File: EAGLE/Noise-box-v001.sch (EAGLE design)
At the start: 20 parts, among them J1 AVR_SPI_PROG_3X22X3_LOCK, J2 BATT, U1 ATMEGA328P_TQFP, U2 MIC5219 3.3V, U3 MCP73831

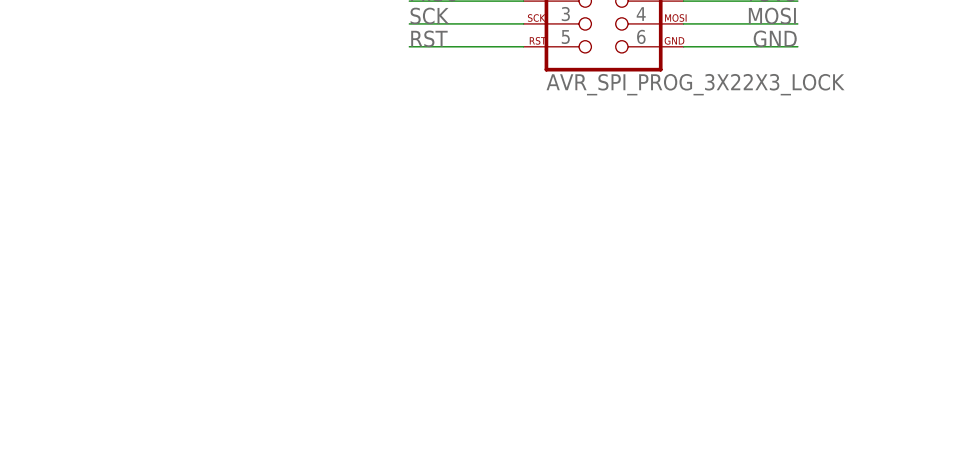
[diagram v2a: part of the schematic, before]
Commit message: Low voltage rail
Added 1.8V rail to accomodate codec IC core
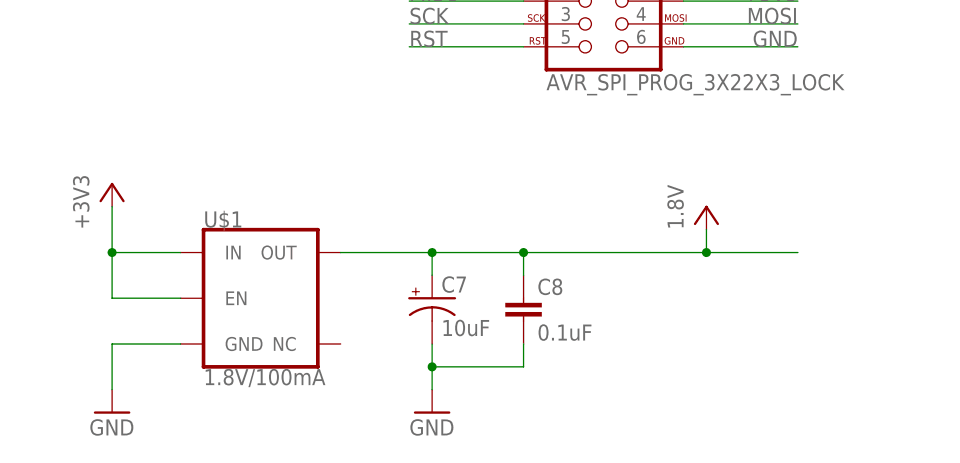
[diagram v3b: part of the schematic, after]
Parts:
- added C7: 10uF, SparkFun-Capacitors:10UF-POLAR-EIA3216-16V-10%(TANT)
- added C8: 0.1uF, SparkFun-Capacitors:0.1UF-0603-25V-5%
- added U$1: 1.8V/100mA, SparkFun-IC-Power:V_REG_SP6214-1.8V
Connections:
- new net VCC: C7.+, C8.1, U$1.OUT
- net +3V3: now also U$1.EN, U$1.IN
- net GND: now also C7.-, C8.2, U$1.GND
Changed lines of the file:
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@@
 <part name="GND7" library="supply1" deviceset="GND" device=""/>
 <part name="GND8" library="supply1" deviceset="GND" device=""/>
+<part name="U$1" library="SparkFun-IC-Power" deviceset="V_REG_SP6214" device="-1.8V" value="1.8V/100mA"/>
+<part name="C7" library="SparkFun-Capacitors" deviceset="10UF-POLAR" device="-EIA3216-16V-10%(TANT)" value="10uF"/>
+<part name="C8" library="SparkFun-Capacitors" deviceset="0.1UF" device="-0603-25V-5%" value="0.1uF"/>
+<part name="GND9" library="supply1" deviceset="GND" device=""/>
+<part name="GND10" library="supply1" deviceset="GND" device=""/>
+<part name="+3V3" library="supply1" deviceset="+3V3" device=""/>
+<part name="P+2" library="supply1" deviceset="VCC" device="" value="1.8V"/>
 </parts>
 <sheets>
@@
 <instance part="GND7" gate="1" x="55.88" y="198.12"/>
 <instance part="GND8" gate="1" x="83.82" y="198.12"/>
+<instance part="U$1" gate="G$1" x="30.48" y="139.7"/>
+<instance part="C7" gate="G$1" x="48.26" y="139.7"/>
+<instance part="C8" gate="G$1" x="58.42" y="137.16"/>
+<instance part="GND9" gate="1" x="12.7" y="127"/>
+<instance part="GND10" gate="1" x="48.26" y="127"/>
+<instance part="+3V3" gate="G$1" x="12.7" y="152.4"/>
+<instance part="P+2" gate="VCC" x="78.74" y="149.86"/>
 </instances>
 <busses>
@@
 <junction x="132.08" y="256.54"/>
 </segment>
+<segment>
+<pinref part="+3V3" gate="G$1" pin="+3V3"/>
+<pinref part="U$1" gate="G$1" pin="IN"/>
+<wire x1="12.7" y1="149.86" x2="12.7" y2="144.78" width="0.1524" layer="91"/>
+<wire x1="12.7" y1="144.78" x2="20.32" y2="144.78" width="0.1524" layer="91"/>
+<pinref part="U$1" gate="G$1" pin="EN"/>
+<wire x1="20.32" y1="139.7" x2="12.7" y2="139.7" width="0.1524" layer="91"/>
+<wire x1="12.7" y1="139.7" x2="12.7" y2="144.78" width="0.1524" layer="91"/>
+<junction x="12.7" y="144.78"/>
+</segment>
 </net>
 <net name="GND" class="0">
@@
 <wire x1="111.76" y1="200.66" x2="101.6" y2="200.66" width="0.1524" layer="91"/>
 <junction x="101.6" y="200.66"/>
+</segment>
+<segment>
+<pinref part="C7" gate="G$1" pin="-"/>
+<pinref part="GND10" gate="1" pin="GND"/>
+<wire x1="48.26" y1="134.62" x2="48.26" y2="132.08" width="0.1524" layer="91"/>
+<pinref part="C8" gate="G$1" pin="2"/>
+<wire x1="48.26" y1="132.08" x2="48.26" y2="129.54" width="0.1524" layer="91"/>
+<wire x1="58.42" y1="134.62" x2="58.42" y2="132.08" width="0.1524" layer="91"/>
+<wire x1="58.42" y1="132.08" x2="48.26" y2="132.08" width="0.1524" layer="91"/>
+<junction x="48.26" y="132.08"/>
+</segment>
+<segment>
+<pinref part="U$1" gate="G$1" pin="GND"/>
+<pinref part="GND9" gate="1" pin="GND"/>
+<wire x1="20.32" y1="134.62" x2="12.7" y2="134.62" width="0.1524" layer="91"/>
+<wire x1="12.7" y1="134.62" x2="12.7" y2="129.54" width="0.1524" layer="91"/>
 </segment>
 </net>
@@
 </segment>
 </net>
+<net name="VCC" class="0">
+<segment>
+<pinref part="U$1" gate="G$1" pin="OUT"/>
+<wire x1="38.1" y1="144.78" x2="48.26" y2="144.78" width="0.1524" layer="91"/>
+<pinref part="C7" gate="G$1" pin="+"/>
+<wire x1="48.26" y1="144.78" x2="58.42" y2="144.78" width="0.1524" layer="91"/>
+<wire x1="58.42" y1="144.78" x2="78.74" y2="144.78" width="0.1524" layer="91"/>
+<wire x1="78.74" y1="144.78" x2="88.9" y2="144.78" width="0.1524" layer="91"/>
+<wire x1="48.26" y1="142.24" x2="48.26" y2="144.78" width="0.1524" layer="91"/>
+<junction x="48.26" y="144.78"/>
+<pinref part="C8" gate="G$1" pin="1"/>
+<wire x1="58.42" y1="142.24" x2="58.42" y2="144.78" width="0.1524" layer="91"/>
+<junction x="58.42" y="144.78"/>
+<pinref part="P+2" gate="VCC" pin="VCC"/>
+<wire x1="78.74" y1="144.78" x2="78.74" y2="147.32" width="0.1524" layer="91"/>
+<junction x="78.74" y="144.78"/>
+</segment>
+</net>

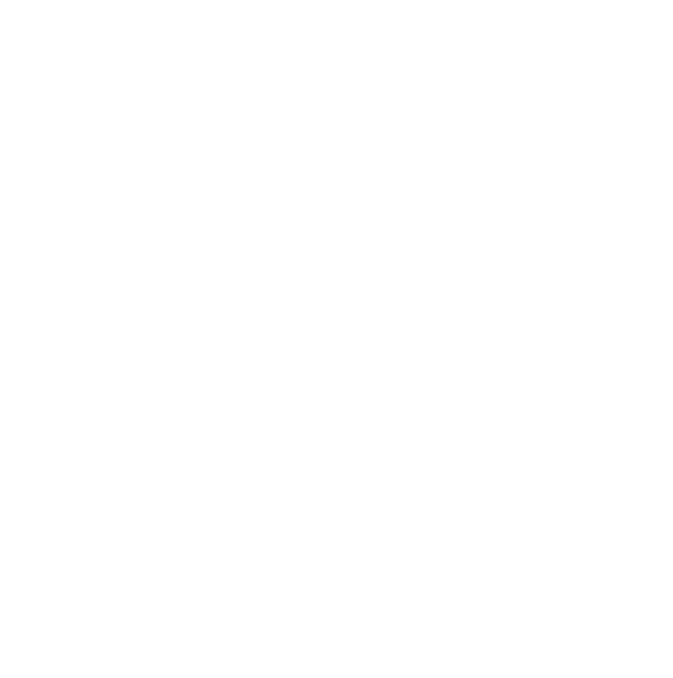
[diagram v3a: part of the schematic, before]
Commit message: micro sd
Added micro sd socket, to hold music tracks
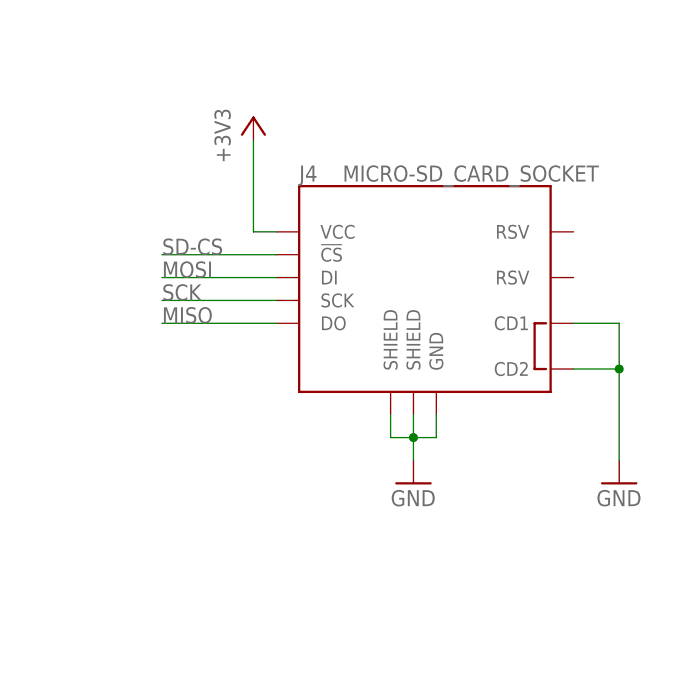
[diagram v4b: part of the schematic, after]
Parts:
- added J4: MICRO-SD_CARD_SOCKET, SparkFun-Connectors:MICRO-SD_CARD_SOCKET
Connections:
- new net SD-CS: J4.!CS
- net +3V3: now also J4.VCC
- net GND: now also J4.CD1, J4.CD2, J4.GND, J4.SHIELD@1, J4.SHIELD@3
- net MISO: now also J4.DO
- net MOSI: now also J4.DI
- net SCK: now also J4.SCK
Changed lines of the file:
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@@
 <part name="+3V3" library="supply1" deviceset="+3V3" device=""/>
 <part name="P+2" library="supply1" deviceset="VCC" device="" value="1.8V"/>
+<part name="J4" library="SparkFun-Connectors" deviceset="MICRO-SD_CARD_SOCKET" device=""/>
+<part name="+3V4" library="supply1" deviceset="+3V3" device=""/>
+<part name="GND11" library="supply1" deviceset="GND" device=""/>
+<part name="GND12" library="supply1" deviceset="GND" device=""/>
 </parts>
 <sheets>
@@
 <instance part="+3V3" gate="G$1" x="12.7" y="152.4"/>
 <instance part="P+2" gate="VCC" x="78.74" y="149.86"/>
+<instance part="J4" gate="1" x="294.64" y="243.84"/>
+<instance part="+3V4" gate="G$1" x="276.86" y="261.62"/>
+<instance part="GND11" gate="1" x="294.64" y="220.98"/>
+<instance part="GND12" gate="1" x="317.5" y="220.98"/>
 </instances>
 <busses>
@@
 <junction x="12.7" y="144.78"/>
 </segment>
+<segment>
+<pinref part="J4" gate="1" pin="VCC"/>
+<wire x1="279.4" y1="248.92" x2="276.86" y2="248.92" width="0.1524" layer="91"/>
+<wire x1="276.86" y1="248.92" x2="276.86" y2="259.08" width="0.1524" layer="91"/>
+<pinref part="+3V4" gate="G$1" pin="+3V3"/>
+</segment>
 </net>
 <net name="GND" class="0">
@@
 <wire x1="12.7" y1="134.62" x2="12.7" y2="129.54" width="0.1524" layer="91"/>
 </segment>
+<segment>
+<pinref part="J4" gate="1" pin="SHIELD@3"/>
+<pinref part="GND11" gate="1" pin="GND"/>
+<wire x1="294.64" y1="228.6" x2="294.64" y2="226.06" width="0.1524" layer="91"/>
+<pinref part="J4" gate="1" pin="GND"/>
+<wire x1="294.64" y1="226.06" x2="294.64" y2="223.52" width="0.1524" layer="91"/>
+<wire x1="297.18" y1="228.6" x2="297.18" y2="226.06" width="0.1524" layer="91"/>
+<wire x1="297.18" y1="226.06" x2="294.64" y2="226.06" width="0.1524" layer="91"/>
+<junction x="294.64" y="226.06"/>
+<pinref part="J4" gate="1" pin="SHIELD@1"/>
+<wire x1="292.1" y1="228.6" x2="292.1" y2="226.06" width="0.1524" layer="91"/>
+<wire x1="292.1" y1="226.06" x2="294.64" y2="226.06" width="0.1524" layer="91"/>
+</segment>
+<segment>
+<pinref part="J4" gate="1" pin="CD1"/>
+<pinref part="GND12" gate="1" pin="GND"/>
+<wire x1="312.42" y1="238.76" x2="317.5" y2="238.76" width="0.1524" layer="91"/>
+<wire x1="317.5" y1="238.76" x2="317.5" y2="233.68" width="0.1524" layer="91"/>
+<pinref part="J4" gate="1" pin="CD2"/>
+<wire x1="317.5" y1="233.68" x2="317.5" y2="223.52" width="0.1524" layer="91"/>
+<wire x1="312.42" y1="233.68" x2="317.5" y2="233.68" width="0.1524" layer="91"/>
+<junction x="317.5" y="233.68"/>
+</segment>
 </net>
 <net name="MOSI" class="0">
@@
 <label x="88.9" y="170.18" size="1.778" layer="95" rot="MR0"/>
 </segment>
+<segment>
+<pinref part="J4" gate="1" pin="DI"/>
+<wire x1="279.4" y1="243.84" x2="266.7" y2="243.84" width="0.1524" layer="91"/>
+<label x="266.7" y="243.84" size="1.778" layer="95"/>
+</segment>
 </net>
 <net name="RST" class="0">
@@
 <label x="45.72" y="170.18" size="1.778" layer="95"/>
 </segment>
+<segment>
+<pinref part="J4" gate="1" pin="SCK"/>
+<wire x1="279.4" y1="241.3" x2="266.7" y2="241.3" width="0.1524" layer="91"/>
+<label x="266.7" y="241.3" size="1.778" layer="95"/>
+</segment>
 </net>
 <net name="MISO" class="0">
@@
 <wire x1="58.42" y1="172.72" x2="45.72" y2="172.72" width="0.1524" layer="91"/>
 <label x="45.72" y="172.72" size="1.778" layer="95"/>
+</segment>
+<segment>
+<pinref part="J4" gate="1" pin="DO"/>
+<wire x1="279.4" y1="238.76" x2="266.7" y2="238.76" width="0.1524" layer="91"/>
+<label x="266.7" y="238.76" size="1.778" layer="95"/>
 </segment>
 </net>
@@
 </segment>
 </net>
+<net name="SD-CS" class="0">
+<segment>
+<pinref part="J4" gate="1" pin="!CS"/>
+<wire x1="279.4" y1="246.38" x2="266.7" y2="246.38" width="0.1524" layer="91"/>
+<label x="266.7" y="246.38" size="1.778" layer="95"/>
+</segment>
+</net>

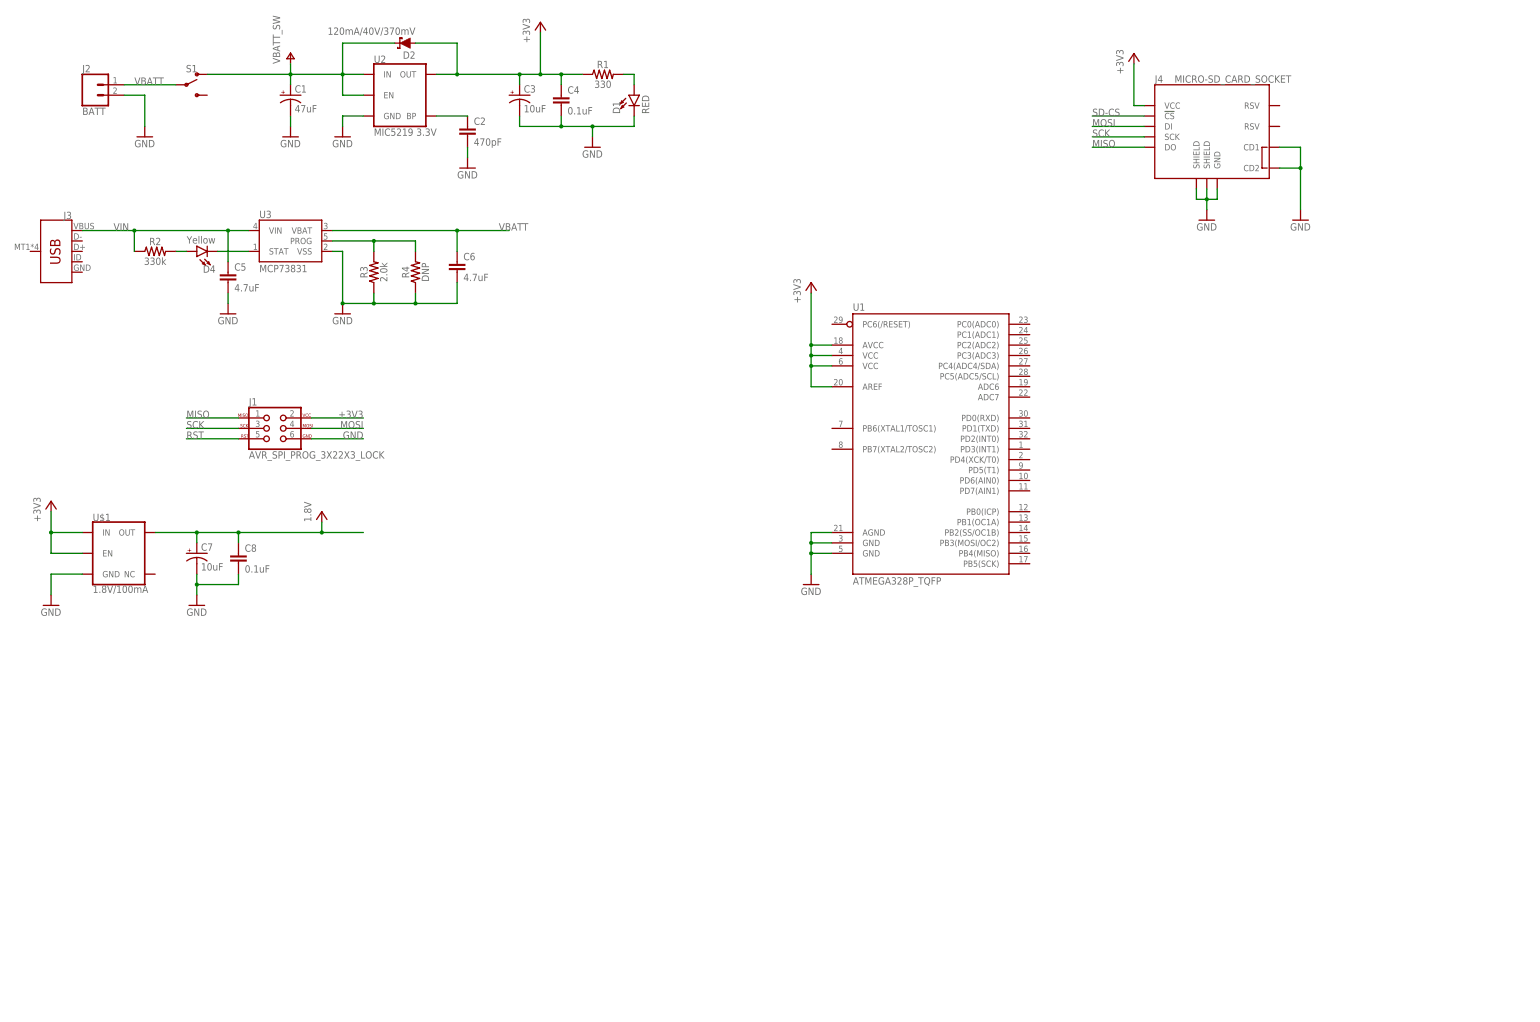
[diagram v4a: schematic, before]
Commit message: mp3 decoder
Added VL1063 codec, headphone jack
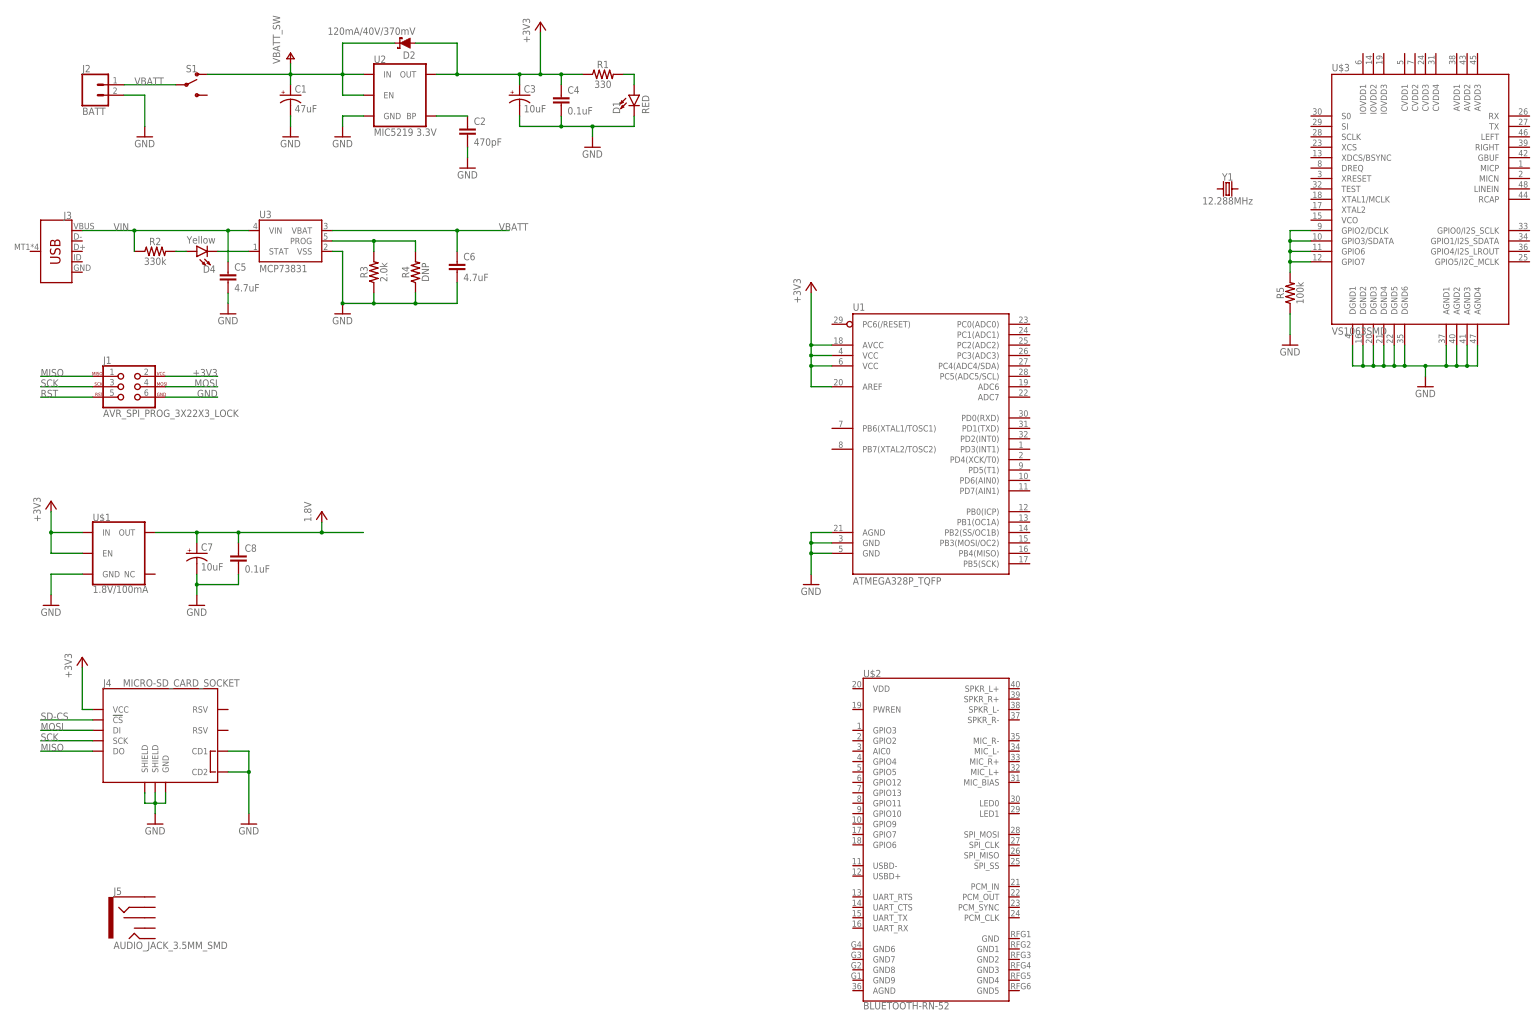
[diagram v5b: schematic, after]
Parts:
- added J5: AUDIO_JACK_3.5MM_SMD, SparkFun-Connectors:AUDIO_JACK_3.5MM_SMD
- added R5: 100k, SparkFun-Resistors:100KOHM-0603-1/10W-1%
- added U$2: BLUETOOTH-RN-52, SparkFun-RF:BLUETOOTH-RN-52
- added U$3: VS1063SMD, SparkFun-IC-Conversion:VS1063SMD
- added Y1: 12.288MHz, SparkFun-Clocks:CRYSTAL-12.288MHZ"
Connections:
- new net N$6: R5.2, U$3.GPIO2/DCLK, U$3.GPIO3/SDATA, U$3.GPIO6, U$3.GPIO7
- net GND: now also R5.1, U$3.AGND1, U$3.AGND2, U$3.AGND3, U$3.AGND4, U$3.DGND1, U$3.DGND2, U$3.DGND3, U$3.DGND4, U$3.DGND5, U$3.DGND6
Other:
- moved on the sheet: J1, J4
